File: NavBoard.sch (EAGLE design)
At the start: 10 parts

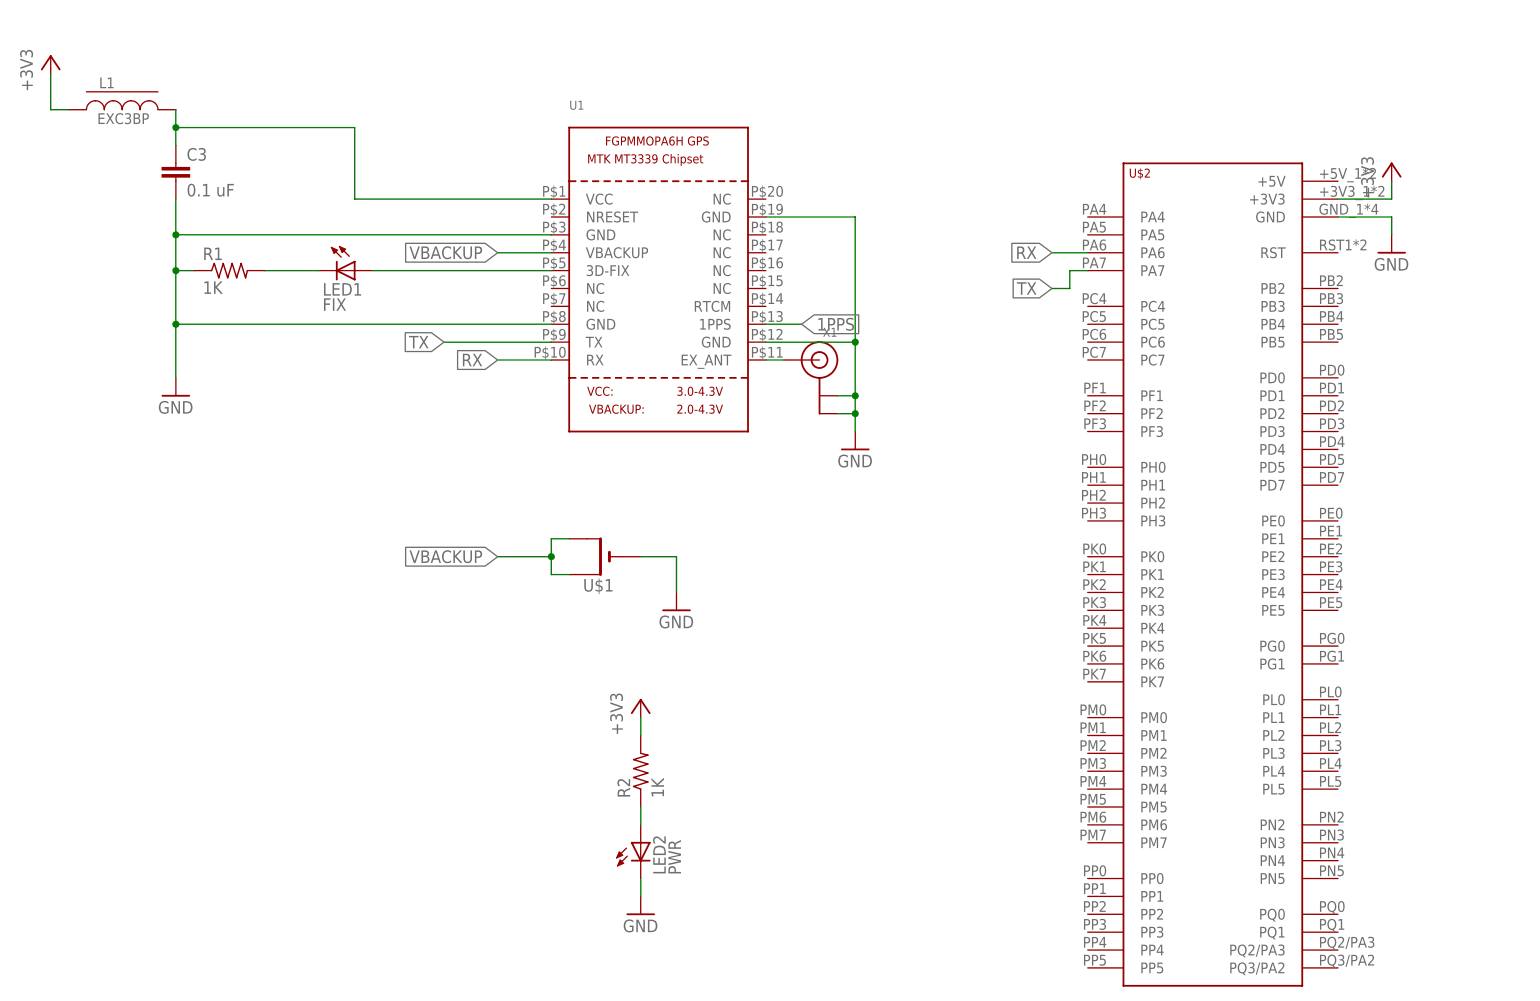
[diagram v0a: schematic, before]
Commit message: Added LSM9DS1 IMU to circuit
Wired up the IMU breakout board to Tiva and changed RX and TX notation
tags to RX(2) and TX(2).
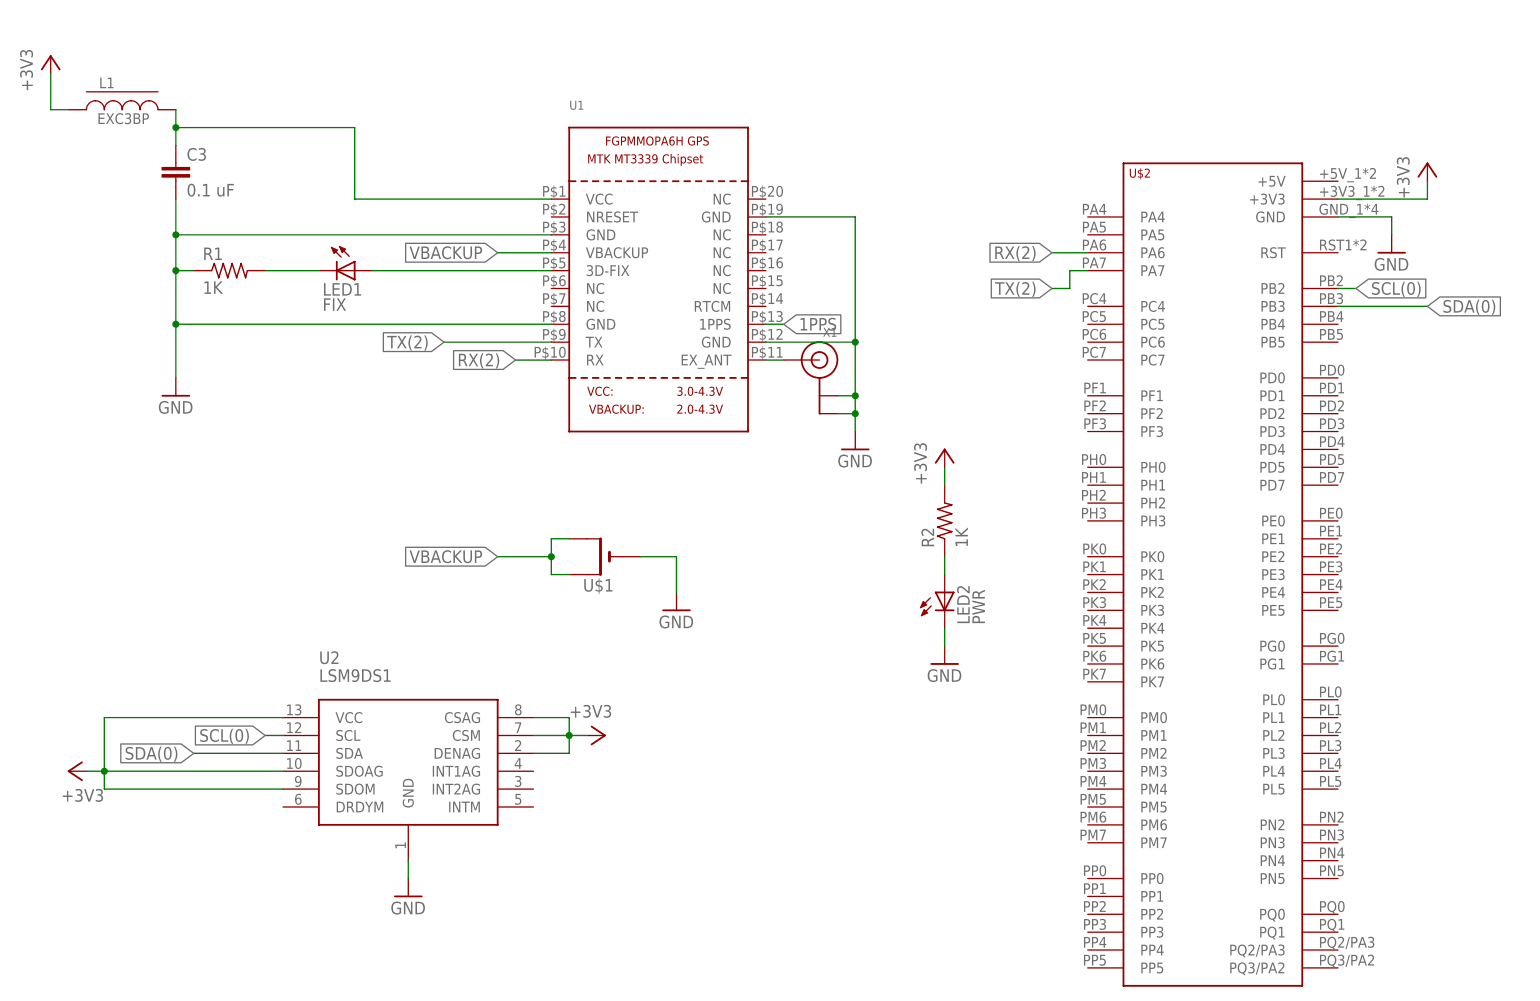
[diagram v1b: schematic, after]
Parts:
- added U2: LSM9DS1, MRDT-Sensors:LSM9DS1
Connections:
- net RX renamed RX(2)
- net TX renamed TX(2)
- new net SCL(0): U$2.PB2, U2.SCL
- new net SDA(0): U$2.PB3, U2.SDA
- net +3V3: now also U2.CSAG, U2.CSM, U2.DENAG, U2.SDOAG, U2.SDOM, U2.VCC
- net GND: now also U2.GND
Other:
- moved on the sheet: LED2, R2
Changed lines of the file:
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@@
 <layers>
 <layer number="1" name="Top" color="4" fill="1" visible="no" active="no"/>
+<layer number="2" name="Route2" color="1" fill="3" visible="no" active="no"/>
+<layer number="3" name="Route3" color="4" fill="3" visible="no" active="no"/>
+<layer number="4" name="Route4" color="1" fill="4" visible="no" active="no"/>
+<layer number="5" name="Route5" color="4" fill="4" visible="no" active="no"/>
+<layer number="6" name="Route6" color="1" fill="8" visible="no" active="no"/>
+<layer number="7" name="Route7" color="4" fill="8" visible="no" active="no"/>
+<layer number="8" name="Route8" color="1" fill="2" visible="no" active="no"/>
+<layer number="9" name="Route9" color="4" fill="2" visible="no" active="no"/>
+<layer number="10" name="Route10" color="1" fill="7" visible="no" active="no"/>
+<layer number="11" name="Route11" color="4" fill="7" visible="no" active="no"/>
+<layer number="12" name="Route12" color="1" fill="5" visible="no" active="no"/>
+<layer number="13" name="Route13" color="4" fill="5" visible="no" active="no"/>
+<layer number="14" name="Route14" color="1" fill="6" visible="no" active="no"/>
+<layer number="15" name="Route15" color="4" fill="6" visible="no" active="no"/>
 <layer number="16" name="Bottom" color="1" fill="1" visible="no" active="no"/>
 <layer number="17" name="Pads" color="2" fill="1" visible="no" active="no"/>
@@
 <part name="+3V1" library="supply1" deviceset="+3V3" device=""/>
 <part name="GND2" library="supply1" deviceset="GND" device=""/>
+<part name="U2" library="MRDT-Sensors" deviceset="LSM9DS1" device=""/>
+<part name="+3V2" library="supply1" deviceset="+3V3" device=""/>
+<part name="+3V5" library="supply1" deviceset="+3V3" device=""/>
+<part name="GND3" library="supply1" deviceset="GND" device=""/>
 </parts>
 <sheets>
@@
 <instance part="GND6" gate="1" x="91.44" y="25.4"/>
 <instance part="LED1" gate="G$1" x="20.32" y="50.8" rot="R270"/>
-<instance part="LED2" gate="G$1" x="60.96" y="-30.48"/>
+<instance part="LED2" gate="G$1" x="104.14" y="5.08"/>
 <instance part="C3" gate="G$1" x="-5.08" y="66.04"/>
 <instance part="R1" gate="G$1" x="2.54" y="50.8"/>
-<instance part="R2" gate="G$1" x="60.96" y="-20.32" rot="R90"/>
-<instance part="+3V4" gate="G$1" x="60.96" y="-10.16"/>
-<instance part="GND7" gate="1" x="60.96" y="-40.64"/>
+<instance part="R2" gate="G$1" x="104.14" y="15.24" rot="R90"/>
+<instance part="+3V4" gate="G$1" x="104.14" y="25.4"/>
+<instance part="GND7" gate="1" x="104.14" y="-5.08"/>
 <instance part="GND8" gate="1" x="-5.08" y="33.02"/>
 <instance part="L1" gate="G$1" x="-12.7" y="73.66"/>
 <instance part="+3V3" gate="G$1" x="-22.86" y="81.28"/>
 <instance part="U$2" gate="G$1" x="129.54" y="-50.8"/>
-<instance part="+3V1" gate="G$1" x="167.64" y="66.04"/>
+<instance part="+3V1" gate="G$1" x="172.72" y="66.04"/>
 <instance part="GND2" gate="1" x="167.64" y="53.34"/>
+<instance part="U2" gate="G$1" x="27.94" y="-20.32"/>
+<instance part="+3V2" gate="G$1" x="-20.32" y="-20.32" rot="R90"/>
+<instance part="+3V5" gate="G$1" x="55.88" y="-15.24" rot="R270"/>
+<instance part="GND3" gate="1" x="27.94" y="-38.1"/>
 </instances>
 <busses>
@@
 <pinref part="GND7" gate="1" pin="GND"/>
 <pinref part="LED2" gate="G$1" pin="C"/>
-<wire x1="60.96" y1="-38.1" x2="60.96" y2="-35.56" width="0.1524" layer="91"/>
+<wire x1="104.14" y1="-2.54" x2="104.14" y2="0" width="0.1524" layer="91"/>
 </segment>
 <segment>
@@
 <wire x1="167.64" y1="58.42" x2="160.02" y2="58.42" width="0.1524" layer="91"/>
 </segment>
-</net>
-<net name="RX" class="0">
-<segment>
-<pinref part="U1" gate="G$1" pin="RX"/>
-<wire x1="48.26" y1="38.1" x2="40.64" y2="38.1" width="0.1524" layer="91"/>
-<label x="40.64" y="38.1" size="1.778" layer="95" rot="R180" xref="yes"/>
-</segment>
-<segment>
-<pinref part="U$2" gate="G$1" pin="PA6"/>
-<wire x1="124.46" y1="53.34" x2="119.38" y2="53.34" width="0.1524" layer="91"/>
-<label x="119.38" y="53.34" size="1.778" layer="95" rot="R180" xref="yes"/>
-</segment>
-</net>
-<net name="TX" class="0">
-<segment>
-<pinref part="U1" gate="G$1" pin="TX"/>
-<wire x1="48.26" y1="40.64" x2="33.02" y2="40.64" width="0.1524" layer="91"/>
-<label x="33.02" y="40.64" size="1.778" layer="95" rot="R180" xref="yes"/>
-</segment>
-<segment>
-<pinref part="U$2" gate="G$1" pin="PA7"/>
-<wire x1="124.46" y1="50.8" x2="121.92" y2="50.8" width="0.1524" layer="91"/>
-<wire x1="121.92" y1="50.8" x2="121.92" y2="48.26" width="0.1524" layer="91"/>
-<wire x1="121.92" y1="48.26" x2="119.38" y2="48.26" width="0.1524" layer="91"/>
-<label x="119.38" y="48.26" size="1.778" layer="95" rot="R180" xref="yes"/>
+<segment>
+<pinref part="U2" gate="G$1" pin="GND"/>
+<pinref part="GND3" gate="1" pin="GND"/>
+<wire x1="27.94" y1="-35.56" x2="27.94" y2="-33.02" width="0.1524" layer="91"/>
 </segment>
 </net>
@@
 <pinref part="+3V4" gate="G$1" pin="+3V3"/>
 <pinref part="R2" gate="G$1" pin="2"/>
-<wire x1="60.96" y1="-15.24" x2="60.96" y2="-12.7" width="0.1524" layer="91"/>
+<wire x1="104.14" y1="20.32" x2="104.14" y2="22.86" width="0.1524" layer="91"/>
 </segment>
 <segment>
@@
 <segment>
 <pinref part="U$2" gate="G$1" pin="+3V3"/>
-<wire x1="160.02" y1="60.96" x2="167.64" y2="60.96" width="0.1524" layer="91"/>
+<wire x1="160.02" y1="60.96" x2="172.72" y2="60.96" width="0.1524" layer="91"/>
 <pinref part="+3V1" gate="G$1" pin="+3V3"/>
-<wire x1="167.64" y1="60.96" x2="167.64" y2="63.5" width="0.1524" layer="91"/>
+<wire x1="172.72" y1="60.96" x2="172.72" y2="63.5" width="0.1524" layer="91"/>
+</segment>
+<segment>
+<pinref part="U2" gate="G$1" pin="SDOM"/>
+<wire x1="10.16" y1="-22.86" x2="-15.24" y2="-22.86" width="0.1524" layer="91"/>
+<wire x1="-15.24" y1="-22.86" x2="-15.24" y2="-20.32" width="0.1524" layer="91"/>
+<pinref part="U2" gate="G$1" pin="SDOAG"/>
+<wire x1="-15.24" y1="-20.32" x2="10.16" y2="-20.32" width="0.1524" layer="91"/>
+<pinref part="U2" gate="G$1" pin="VCC"/>
+<wire x1="10.16" y1="-12.7" x2="-15.24" y2="-12.7" width="0.1524" layer="91"/>
+<wire x1="-15.24" y1="-12.7" x2="-15.24" y2="-20.32" width="0.1524" layer="91"/>
+<junction x="-15.24" y="-20.32"/>
+<pinref part="+3V2" gate="G$1" pin="+3V3"/>
+<wire x1="-17.78" y1="-20.32" x2="-15.24" y2="-20.32" width="0.1524" layer="91"/>
+</segment>
+<segment>
+<pinref part="U2" gate="G$1" pin="DENAG"/>
+<wire x1="45.72" y1="-17.78" x2="50.8" y2="-17.78" width="0.1524" layer="91"/>
+<pinref part="U2" gate="G$1" pin="CSM"/>
+<wire x1="45.72" y1="-15.24" x2="50.8" y2="-15.24" width="0.1524" layer="91"/>
+<wire x1="50.8" y1="-15.24" x2="50.8" y2="-17.78" width="0.1524" layer="91"/>
+<pinref part="U2" gate="G$1" pin="CSAG"/>
+<wire x1="45.72" y1="-12.7" x2="50.8" y2="-12.7" width="0.1524" layer="91"/>
+<wire x1="50.8" y1="-12.7" x2="50.8" y2="-15.24" width="0.1524" layer="91"/>
+<junction x="50.8" y="-15.24"/>
+<pinref part="+3V5" gate="G$1" pin="+3V3"/>
+<wire x1="53.34" y1="-15.24" x2="50.8" y2="-15.24" width="0.1524" layer="91"/>
 </segment>
 </net>
@@
 <pinref part="R2" gate="G$1" pin="1"/>
 <pinref part="LED2" gate="G$1" pin="A"/>
-<wire x1="60.96" y1="-27.94" x2="60.96" y2="-25.4" width="0.1524" layer="91"/>
+<wire x1="104.14" y1="7.62" x2="104.14" y2="10.16" width="0.1524" layer="91"/>
 </segment>
 </net>
@@
 <segment>
 <pinref part="U1" gate="G$1" pin="1PPS"/>
-<wire x1="78.74" y1="43.18" x2="83.82" y2="43.18" width="0.1524" layer="91"/>
-<label x="83.82" y="43.18" size="1.778" layer="95" xref="yes"/>
-</segment>
-</net>
+<wire x1="78.74" y1="43.18" x2="81.28" y2="43.18" width="0.1524" layer="91"/>
+<label x="81.28" y="43.18" size="1.778" layer="95" xref="yes"/>
+</segment>
+</net>
+<net name="SCL(0)" class="0">
+<segment>
+<pinref part="U$2" gate="G$1" pin="PB2"/>
+<wire x1="160.02" y1="48.26" x2="162.56" y2="48.26" width="0.1524" layer="91"/>
+<label x="162.56" y="48.26" size="1.778" layer="95" xref="yes"/>
+</segment>
+<segment>
+<pinref part="U2" gate="G$1" pin="SCL"/>
+<wire x1="10.16" y1="-15.24" x2="7.62" y2="-15.24" width="0.1524" layer="91"/>
+<label x="7.62" y="-15.24" size="1.778" layer="95" rot="R180" xref="yes"/>
+</segment>
+</net>
+<net name="SDA(0)" class="0">
+<segment>
+<pinref part="U$2" gate="G$1" pin="PB3"/>
+<wire x1="160.02" y1="45.72" x2="172.72" y2="45.72" width="0.1524" layer="91"/>
+<label x="172.72" y="45.72" size="1.778" layer="95" xref="yes"/>
+</segment>
+<segment>
+<pinref part="U2" gate="G$1" pin="SDA"/>
+<wire x1="10.16" y1="-17.78" x2="-2.54" y2="-17.78" width="0.1524" layer="91"/>
+<label x="-2.54" y="-17.78" size="1.778" layer="95" rot="R180" xref="yes"/>
+</segment>
+</net>
+<net name="RX(2)" class="0">
+<segment>
+<pinref part="U$2" gate="G$1" pin="PA6"/>
+<wire x1="124.46" y1="53.34" x2="119.38" y2="53.34" width="0.1524" layer="91"/>
+<label x="119.38" y="53.34" size="1.778" layer="95" rot="R180" xref="yes"/>
+</segment>
+<segment>
+<pinref part="U1" gate="G$1" pin="RX"/>
+<wire x1="48.26" y1="38.1" x2="43.18" y2="38.1" width="0.1524" layer="91"/>
+<label x="43.18" y="38.1" size="1.778" layer="95" rot="R180" xref="yes"/>
+</segment>
+</net>
+<net name="TX(2)" class="0">
+<segment>
+<pinref part="U$2" gate="G$1" pin="PA7"/>
+<wire x1="124.46" y1="50.8" x2="121.92" y2="50.8" width="0.1524" layer="91"/>
+<wire x1="121.92" y1="50.8" x2="121.92" y2="48.26" width="0.1524" layer="91"/>
+<wire x1="121.92" y1="48.26" x2="119.38" y2="48.26" width="0.1524" layer="91"/>
+<label x="119.38" y="48.26" size="1.778" layer="95" rot="R180" xref="yes"/>
+</segment>
+<segment>
+<pinref part="U1" gate="G$1" pin="TX"/>
+<wire x1="48.26" y1="40.64" x2="33.02" y2="40.64" width="0.1524" layer="91"/>
+<label x="33.02" y="40.64" size="1.778" layer="95" rot="R180" xref="yes"/>
+</segment>
+</net>
